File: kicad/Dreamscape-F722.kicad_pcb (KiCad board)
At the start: 4 copper layers, 40 x 40 mm, 111 parts, among them J1 From BEC, J10 PA4, J11 PB2, J12 PC11, J13 PC10, J14 PB6, J15 PB7, J16 PA9, J17 PA10, J18 PA2, J19 PA3, J2 BZ+, J20 PB10, J21 PB11, J22 USB_C_Receptacle_USB2.0_14P, J23 SWDIO, J24 SWCLK, J25 Conn_01x01, J26 Conn_01x01, J27 Conn_01x01, J28 PA0, J29 PA1, J3 COL, J30 Conn_01x01, J31 Conn_01x01, J32 Conn_01x01, J33 Conn_01x01, J34 Conn_01x01, J35 Conn_01x01, J36 Conn_01x01, J37 Conn_01x01, J38 Conn_01x01, J39 Conn_01x01, J4 PA7, J40 Conn_01x01, J41 Conn_01x01, J42 Conn_01x01, J43 Conn_01x01, J44 Conn_01x01, J5 PA6, J6 PA5, J7 PC1, J8 PC11, J9 PB13, Q1 AO3401A, Q2 BC817, SW1 SW_SPST, SW2 SW_SPST, U1 STM32F722RET6, U2 TLV75733PDRV, U3 TPD2EUSB30, U4 ICM-42688-P, U5 BMP280, Y1 8MHz, Y2 32.768KHz

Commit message: optimise traces
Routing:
- net +5V: track 37.9 -> 39.4 mm, vias 3 -> 5

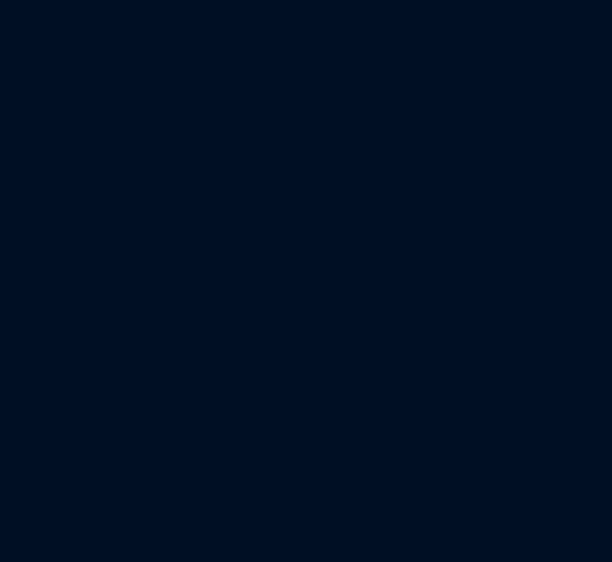
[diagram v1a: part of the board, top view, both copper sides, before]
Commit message: add diodes to pcb (wiring tomorrow)
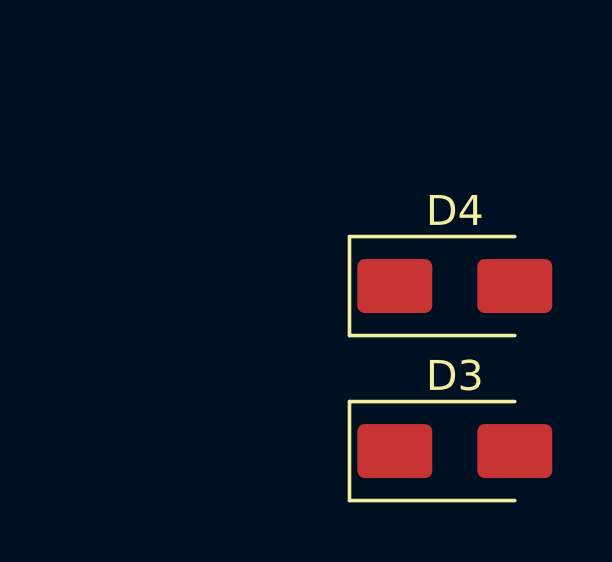
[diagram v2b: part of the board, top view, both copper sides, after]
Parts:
- added D3: SS14, Diode_SMD:D_SMA, F.Cu at (77.5, 60.8)
- added D4: SS14, Diode_SMD:D_SMA, F.Cu at (77.5, 55.2)
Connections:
- net VBUS renamed Net-(D4-A)
- J2 pad 1: +5V -> Net-(D3-A)

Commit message: update repos
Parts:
- D3, D4: moved to B.Cu
- moved D4 38.3 mm to (48.8, 30.0)
- moved D3 36.6 mm to (46.5, 41.2), turned to 90 degrees
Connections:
- J2 pad 1: Net-(D3-A) -> +5V
- Q1 pad 3: +5V -> Net-(D3-A)
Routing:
- net +5V: track 39.4 -> 41.0 mm, vias 5 -> 4
- net Net-(D4-A): track 6.57 -> 7.44 mm, vias 0 -> 1
- net I2C1_SDA: track 22.9 -> 23.4 mm
- net Net-(D3-A): vias 0 -> 1
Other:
- board text added: "JLCJLCJLCJLC"

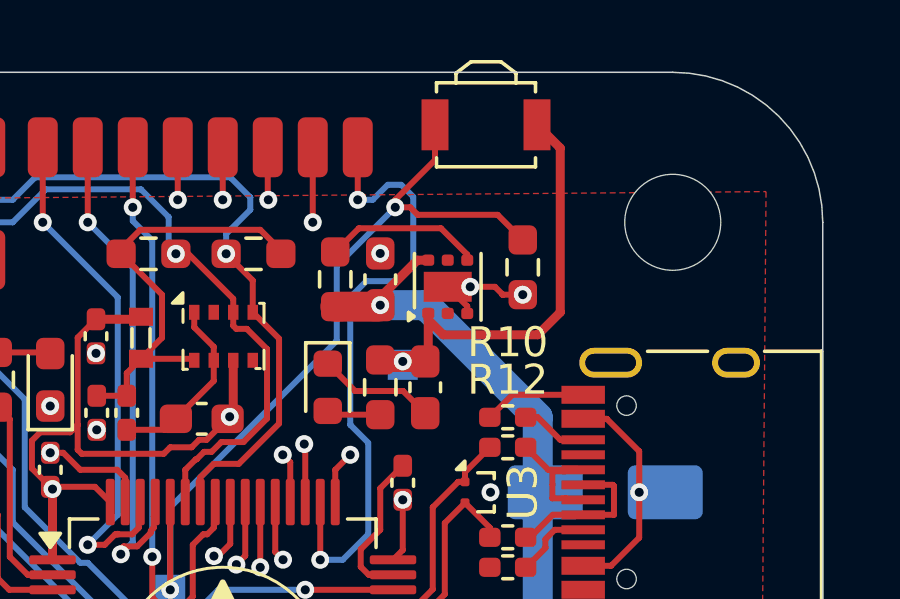
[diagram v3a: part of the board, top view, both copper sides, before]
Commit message: change ldo to hand-solderable type
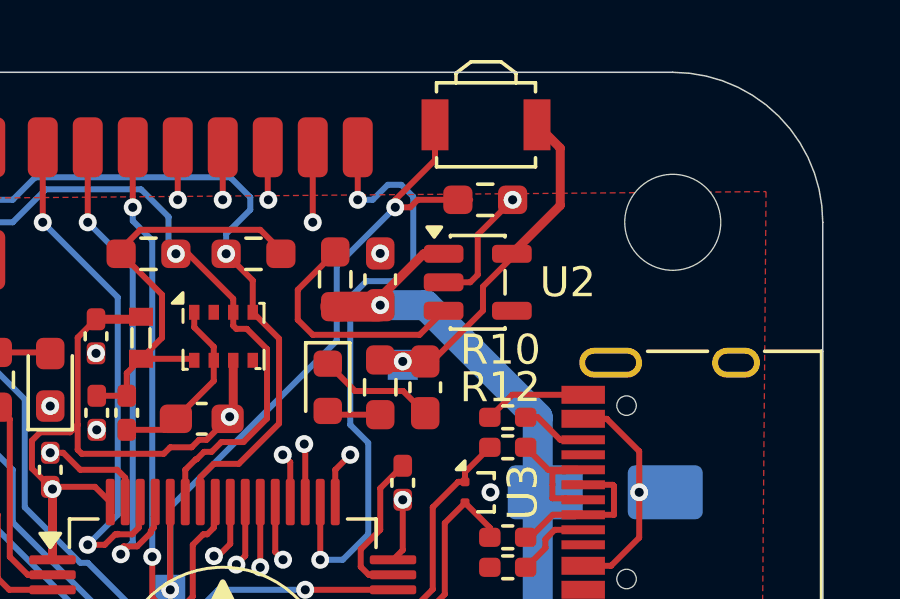
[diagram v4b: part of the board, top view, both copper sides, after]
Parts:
- U2: value TLV75733PDRV -> TLV75733PDBV; footprint Package_SON:WSON-6-1EP_2x2mm_P0.65mm_EP1x1.6mm -> Package_TO_SOT_SMD:SOT-23-5
- moved R2 2.57 mm to (44.8, 20.2), turned to 0 degrees
- moved U2 1.01 mm to (44.5, 23.0), turned to 0 degrees
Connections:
- U2 pad 1: +3.3V -> +5V
- U2 pad 2: unconnected-(U2-NC-Pad2) -> GND
- U2 pad 3: GND -> Net-(U2-EN)
- U2 pad 4: Net-(U2-EN) -> unconnected-(U2-NC-Pad4)
- U2 pad 5: unconnected-(U2-NC-Pad5) -> +3.3V
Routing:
- net Net-(U2-EN): track 5.28 -> 8.18 mm
- net BOOT0: track 26.8 -> 24.7 mm
- net +3.3V: track 81.9 -> 80.1 mm
- net +5V: track 41.0 -> 41.6 mm
- net GND: track 57.2 -> 57.6 mm, vias 18 -> 17
